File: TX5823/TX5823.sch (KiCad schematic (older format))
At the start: 94 parts, among them IC1 ATMEGA328P-A, IC2 ATTINY13A-SS, P1 Akku_in, P2 ISP, P3 Mavlink, P4 CONN_01X01, P5 CONN_01X01, P6 CONN_01X01, P7 CONN_01X01, Q1 MOSFET_P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

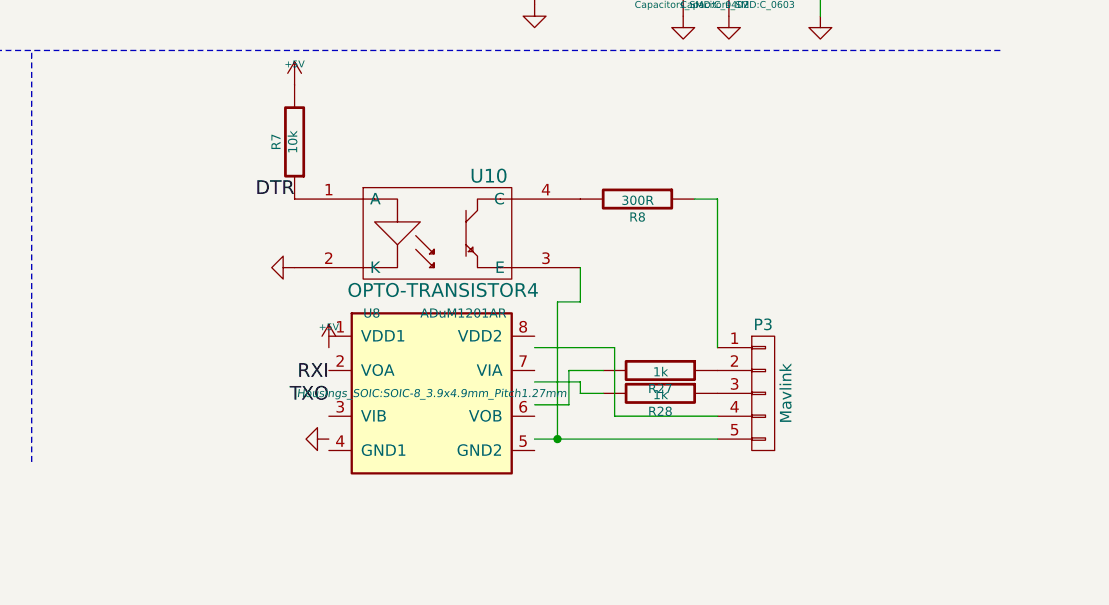
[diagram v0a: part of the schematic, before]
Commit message: mavlink und adum geroutet
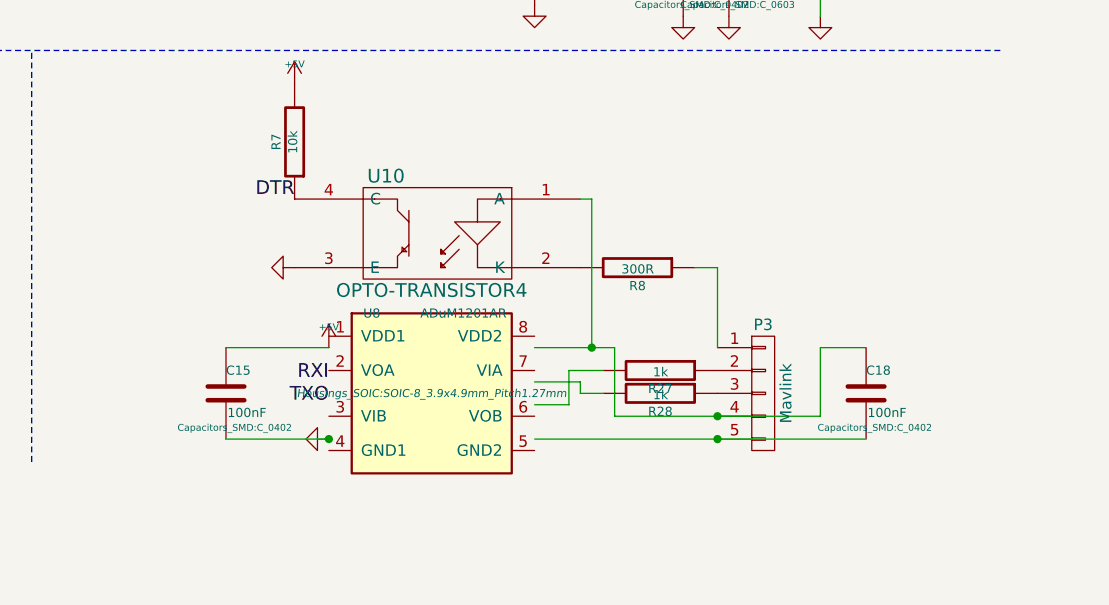
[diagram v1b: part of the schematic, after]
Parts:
- added C15, C18: 100nF, Capacitors_SMD:C_0402, symbol C
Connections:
- net +5V: now also C15.1
- net DTR: now also U10.4 (C); no longer U10.1 (A)
- net GND: now also U10.3 (E), C15.2; no longer U10.2 (K)
- net at P3.4 (P4): now also U10.1 (A), C18.1
- net at P3.5 (P5): now also C18.2; no longer U10.3 (E)
- net at R8.2: now also U10.2 (K); no longer U10.4 (C)
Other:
- moved on the sheet: R8
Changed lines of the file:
@@
 	14150 9500 14300 9500
 Wire Wire Line
-	14800 9700 14350 9700
+	14350 9700 15250 9700
 Wire Wire Line
 	14350 9700 14350 9400
@@
 	14350 9400 14000 9400
 Wire Wire Line
-	14800 9800 14000 9800
+	14000 9800 15450 9800
 $Comp
 L +5V #PWR094
@@
 L OPTO-TRANSISTOR4 U10
 U 1 1 55216F1B
-P 13600 8900
-F 0 "U10" H 13800 9150 60  0000 C CNN
-F 1 "OPTO-TRANSISTOR4" H 13600 8650 60  0000 C CNN
-F 2 "toni:SO-4" H 13600 8900 60  0001 C CNN
-F 3 "" H 13600 8900 60  0000 C CNN
-	1    13600 8900
-	1    0    0    -1
+P 13550 8900
+F 0 "U10" H 13750 9150 60  0000 C CNN
+F 1 "OPTO-TRANSISTOR4" H 13550 8650 60  0000 C CNN
+F 2 "toni:SO-4" H 13550 8900 60  0001 C CNN
+F 3 "" H 13550 8900 60  0000 C CNN
+	1    13550 8900
+	-1   0    0    -1
 $EndComp
 $Comp
 L R R8
 U 1 1 5521767B
-P 14450 8750
-F 0 "R8" V 14530 8750 40  0000 C CNN
-F 1 "300R" V 14457 8751 40  0000 C CNN
-F 2 "Resistors_SMD:R_0603" V 14380 8750 30  0001 C CNN
-F 3 "" V 14530 8750 30  0000 C CNN
-	1    14450 8750
+P 14450 9050
+F 0 "R8" V 14530 9050 40  0000 C CNN
+F 1 "300R" V 14457 9051 40  0000 C CNN
+F 2 "Resistors_SMD:R_0603" V 14380 9050 30  0001 C CNN
+F 3 "" V 14530 9050 30  0000 C CNN
+	1    14450 9050
 	0    1    1    0
 $EndComp
-Wire Wire Line
-	14700 8750 14800 8750
-Wire Wire Line
-	14800 8750 14800 9400
 $Comp
 L R R7
@@
 $EndComp
 Wire Wire Line
-	14200 9050 14200 9200
+	14700 9050 14800 9050
 Wire Wire Line
-	14200 9200 14100 9200
+	14800 9050 14800 9400
 Wire Wire Line
-	14100 9200 14100 9800
-Connection ~ 14100 9800
+	14200 8750 14250 8750
+Wire Wire Line
+	14250 8750 14250 9400
+Connection ~ 14250 9400
+$Comp
+L C C15
+U 1 1 55218CA9
+P 12650 9600
+F 0 "C15" H 12650 9700 40  0000 L CNN
+F 1 "100nF" H 12656 9515 40  0000 L CNN
+F 2 "Capacitors_SMD:C_0402" H 12688 9450 30  0000 C CNN
+F 3 "" H 12650 9600 60  0000 C CNN
+	1    12650 9600
+	1    0    0    -1
+$EndComp
+$Comp
+L C C18
+U 1 1 552191D8
+P 15450 9600
+F 0 "C18" H 15450 9700 40  0000 L CNN
+F 1 "100nF" H 15456 9515 40  0000 L CNN
+F 2 "Capacitors_SMD:C_0402" H 15488 9450 30  0000 C CNN
+F 3 "" H 15450 9600 60  0000 C CNN
+	1    15450 9600
+	1    0    0    -1
+$EndComp
+Connection ~ 14800 9800
+Wire Wire Line
+	15250 9700 15250 9400
+Wire Wire Line
+	15250 9400 15450 9400
+Connection ~ 14800 9700
+Wire Wire Line
+	12650 9800 13100 9800
+Wire Wire Line
+	12650 9400 13100 9400
+Connection ~ 13100 9800
 $EndSCHEMATC

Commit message: Neue Fertigungsdateien hinzugefügt
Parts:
- added D3: ZENER, Diodes_SMD:Diode-SMB_Standard, symbol ZENER
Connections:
- net Akku+: now also D3.2 (K)
- net GND: now also D3.1 (A)
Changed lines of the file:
@@
 	12650 9400 13100 9400
 Connection ~ 13100 9800
+$Comp
+L ZENER D3
+U 1 1 55218752
+P 4050 4150
+F 0 "D3" H 4050 4250 50  0000 C CNN
+F 1 "ZENER" H 4050 4050 40  0000 C CNN
+F 2 "Diodes_SMD:Diode-SMB_Standard" H 4050 4150 60  0001 C CNN
+F 3 "" H 4050 4150 60  0000 C CNN
+	1    4050 4150
+	0    -1   -1   0
+$EndComp
+$Comp
+L GND #PWR097
+U 1 1 5521BABA
+P 4050 4350
+F 0 "#PWR097" H 4050 4350 30  0001 C CNN
+F 1 "GND" H 4050 4280 30  0001 C CNN
+F 2 "" H 4050 4350 60  0000 C CNN
+F 3 "" H 4050 4350 60  0000 C CNN
+	1    4050 4350
+	1    0    0    -1
+$EndComp
+Wire Wire Line
+	3400 3950 4050 3950
 $EndSCHEMATC

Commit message: fertigungsdaten, gerberfiles und attiny13a programm hinzugefügt
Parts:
- D3: value ZENER -> P6SMB 27A SMD
- Q1: Teilenummer FDS6982AS -> FDS4141
- R18, R31, R8: value 300R -> 330R
- U8: value ADuM1201AR -> ADuM7241 ARZ
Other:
- note added: "MOSFET falsch herum\nWorkaround:\nR3 ersetzen durch ferritperele mit nummer 742792150\nRestlicher Teil von Softstart unbestückt lassen"
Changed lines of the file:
@@
 F 1 "MOSFET_N" H 12560 3650 60  0000 R CNN
 F 2 "toni:SOT23_GDS" H 12550 3800 60  0001 C CNN
-F 3 "" H 12550 3800 60  0000 C CNN
+F 3 "IRML2502" H 12550 3800 60  0000 C CNN
 	1    12550 3800
 	1    0    0    -1
@@
 F 1 "INDUCTOR" V 4900 8100 40  0000 C CNN
 F 2 "Choke_SMD:Choke_SMD_Wuerth-WE-PD-Typ-LS_Handsoldering" H 4800 8100 60  0001 C CNN
-F 3 "" H 4800 8100 60  0000 C CNN
+F 3 "WE-LHMI 1335 4,7uH 8,5A" H 4800 8100 60  0000 C CNN
 	1    4800 8100
 	0    -1   -1   0
@@
 P 8700 8900
 F 0 "R18" V 8780 8900 40  0000 C CNN
-F 1 "300R" V 8707 8901 40  0000 C CNN
+F 1 "330R" V 8707 8901 40  0000 C CNN
 F 2 "Resistors_SMD:R_0805" V 8630 8900 30  0001 C CNN
 F 3 "" V 8780 8900 30  0000 C CNN
@@
 P 10450 8650
 F 0 "R31" V 10530 8650 40  0000 C CNN
-F 1 "300R" V 10457 8651 40  0000 C CNN
+F 1 "330R" V 10457 8651 40  0000 C CNN
 F 2 "Capacitors_SMD:C_0805" V 10380 8650 30  0001 C CNN
 F 3 "" V 10530 8650 30  0000 C CNN
@@
 F 2 "toni:SO8_WITH_EP" H 3300 4300 60  0001 C CNN
 F 3 "" H 3300 4300 60  0000 C CNN
-F 4 "FDS6982AS" H 3300 4300 60  0001 C CNN "Teilenummer"
+F 4 "FDS4141" H 3300 4300 60  0001 C CNN "Teilenummer"
 	1    3300 4300
 	1    0    0    -1
@@
 P 13550 9600
 F 0 "U8" H 13250 9950 40  0000 L CNN
-F 1 "ADuM1201AR" H 13500 9950 40  0000 L CNN
+F 1 "ADuM7241 ARZ" H 13500 9950 40  0000 L CNN
 F 2 "Housings_SOIC:SOIC-8_3.9x4.9mm_Pitch1.27mm" H 13550 9600 35  0000 C CIN
 F 3 "" H 13550 9600 60  0000 C CNN
@@
 P 14450 9050
 F 0 "R8" V 14530 9050 40  0000 C CNN
-F 1 "300R" V 14457 9051 40  0000 C CNN
+F 1 "330R" V 14457 9051 40  0000 C CNN
 F 2 "Resistors_SMD:R_0603" V 14380 9050 30  0001 C CNN
 F 3 "" V 14530 9050 30  0000 C CNN
@@
 P 4050 4150
 F 0 "D3" H 4050 4250 50  0000 C CNN
-F 1 "ZENER" H 4050 4050 40  0000 C CNN
+F 1 "P6SMB 27A SMD" H 4050 4050 40  0000 C CNN
 F 2 "Diodes_SMD:Diode-SMB_Standard" H 4050 4150 60  0001 C CNN
 F 3 "" H 4050 4150 60  0000 C CNN
@@
 Wire Wire Line
 	3400 3950 4050 3950
+Text Notes 4500 3900 0    60   ~ 0
+MOSFET falsch herum\nWorkaround:\nR3 ersetzen durch ferritperele mit nummer 742792150\nRestlicher Teil von Softstart unbestückt lassen
 $EndSCHEMATC
